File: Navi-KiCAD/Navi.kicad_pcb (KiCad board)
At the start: 4 copper layers, 50 x 40 mm, 203 parts, among them J1 AXK5S80047YG, J2 AXK5S80047YG, J3 473460001, J4 0734120110, J5 0734120110, J6 0734120110, U1 CC1310F128RGZR, U10 Logo, U11 Logo, U12 ATSAME70Q21A-AN, U13 NUF2042XV6T1G, U2 CC1190RGVR, U3 CC2650F128RGZR, U4 CC2592RGVR, U5 MPU-9250, U6 LP5521YQ/NOPB, U7 LPS25HBTR, U8 TPS54232DR, U9 MAX-M8W-0, Y1 9HT11-32.768KDZB-T, Y2 7V-16.000MAHJ-T, Y3 XRCGB24M000F2P00R0, Y5 XRCGB24M000F2P00R0

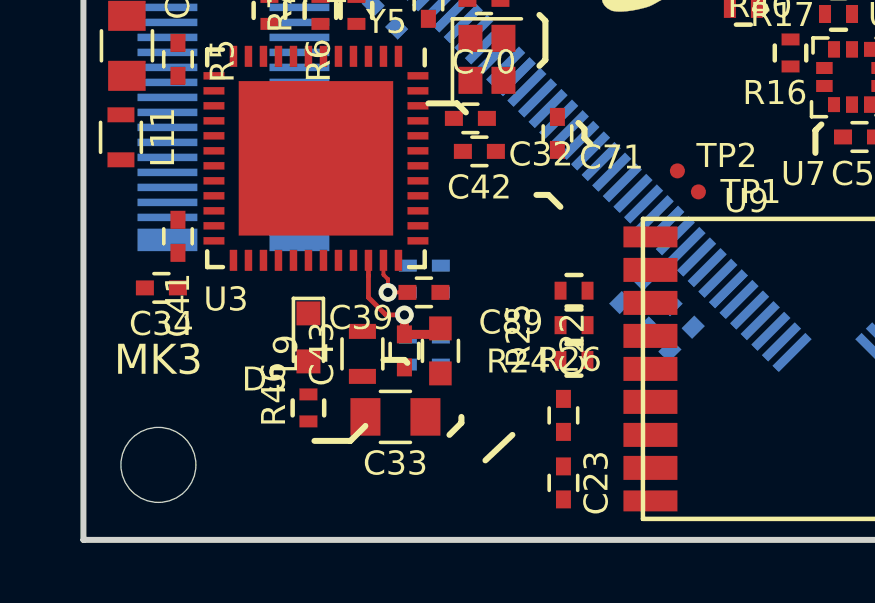
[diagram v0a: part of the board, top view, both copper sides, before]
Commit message: Some BOM consolidation.
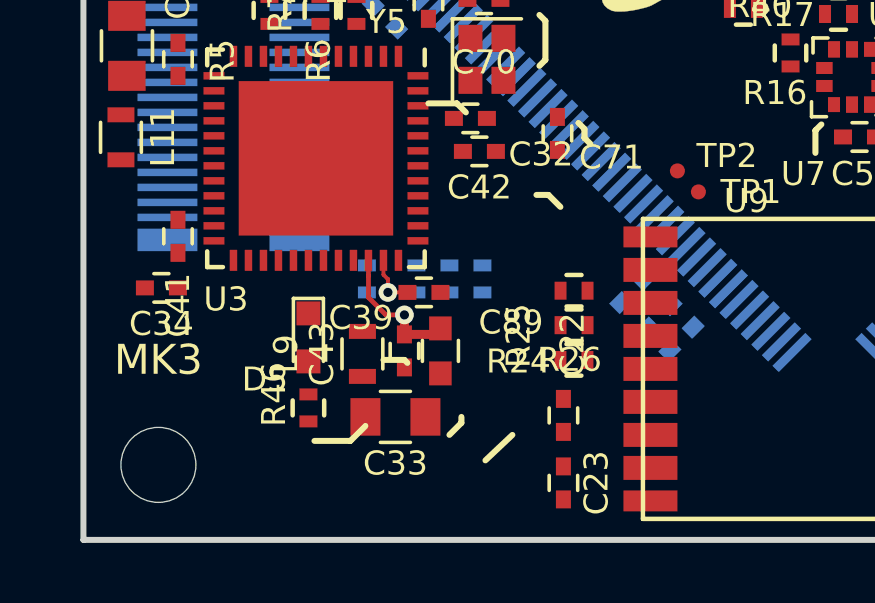
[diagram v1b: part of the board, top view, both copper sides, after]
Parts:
- R40, R41: value DNP -> 0 DNP
- moved U10 28.1 mm to (60.2, 117.8)
- moved R32 2.78 mm to (63.3, 116.3), turned to 270 degrees
- moved R36 2.77 mm to (59.5, 116.3), turned to 90 degrees
- moved R34 0.29 mm to (61.1, 116.3)
- moved R33 0.28 mm to (62.2, 116.3)
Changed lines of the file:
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@@
     (pad 1 np_thru_hole circle (at 0 0) (size 2.5 2.5) (drill 2.5) (layers *.Cu *.Mask))
   )
-  (module Connectors:AXK5S80047YG locked (layer B.Cu)
+  (module Connectors:AXK5S80047YG (layer B.Cu)
     (at 95 105 90)
     (descr AXK5S80047YG)
@@
   )
   (module Symbols:NaviLOGO (layer B.Cu)
-    (at 88.3 118 230)
+    (at 60.2 117.75 230)
     (attr virtual)
     (fp_text reference U10 (at 0 0 230) (layer B.SilkS) hide
@@
       (effects (font (size 0.8 0.8) (thickness 0.13)))
     )
-    (fp_text value DNP (at 0 1.8 180) (layer F.Fab)
+    (fp_text value "0 DNP" (at 0 1.8 180) (layer F.Fab)
       (effects (font (size 1 1) (thickness 0.15)))
     )
@@
       (effects (font (size 0.8 0.8) (thickness 0.13)))
     )
-    (fp_text value DNP (at 0 1.8 180) (layer F.Fab)
+    (fp_text value "0 DNP" (at 0 1.8 180) (layer F.Fab)
       (effects (font (size 1 1) (thickness 0.15)))
     )
@@
   )
   (module Resistors_SMD:R_0402 (layer B.Cu)
-    (at 60.815017 116.307166 270)
+    (at 61.1 116.3 270)
     (descr "Resistor SMD 0402, reflow soldering, Vishay (see dcrcw.pdf)")
     (tags "resistor 0402")
@@
   )
   (module Resistors_SMD:R_0402 (layer B.Cu)
-    (at 61.915018 118.706889 90)
+    (at 63.3 116.3 270)
     (descr "Resistor SMD 0402, reflow soldering, Vishay (see dcrcw.pdf)")
     (tags "resistor 0402")
     (attr smd)
-    (fp_text reference R32 (at 1.949723 0.050526 90) (layer B.SilkS)
+    (fp_text reference R32 (at 1.949723 0.050526 270) (layer B.SilkS)
       (effects (font (size 0.8 0.8) (thickness 0.13)) (justify mirror))
     )
-    (fp_text value 1k (at 0 -1.8 90) (layer B.Fab)
+    (fp_text value 1k (at 0 -1.8 270) (layer B.Fab)
       (effects (font (size 0.9 0.9) (thickness 0.1)) (justify mirror))
     )
@@
     (fp_line (start 0.5 -0.25) (end -0.5 -0.25) (layer B.Fab) (width 0.1))
     (fp_line (start -0.5 -0.25) (end -0.5 0.25) (layer B.Fab) (width 0.1))
-    (pad 2 smd rect (at 0.45 0 90) (size 0.4 0.6) (layers B.Cu B.Paste B.Mask)
+    (pad 2 smd rect (at 0.45 0 270) (size 0.4 0.6) (layers B.Cu B.Paste B.Mask)
       (net 92 "/2.4 GHz Radio/~RESET"))
-    (pad 1 smd rect (at -0.45 0 90) (size 0.4 0.6) (layers B.Cu B.Paste B.Mask)
+    (pad 1 smd rect (at -0.45 0 270) (size 0.4 0.6) (layers B.Cu B.Paste B.Mask)
       (net 118 /2.4_RESET_EXT))
     (model Resistors_SMD.3dshapes/R_0402.wrl
@@
   )
   (module Resistors_SMD:R_0402 (layer B.Cu)
-    (at 60.815017 118.706889 270)
+    (at 59.45 116.3 90)
     (descr "Resistor SMD 0402, reflow soldering, Vishay (see dcrcw.pdf)")
     (tags "resistor 0402")
     (attr smd)
-    (fp_text reference R36 (at 2.000277 -2.050526 270) (layer B.SilkS)
+    (fp_text reference R36 (at 2.000277 -2.050526 90) (layer B.SilkS)
       (effects (font (size 0.8 0.8) (thickness 0.13)) (justify mirror))
     )
-    (fp_text value 100k (at 0 -1.8 270) (layer B.Fab)
+    (fp_text value 100k (at 0 -1.8 90) (layer B.Fab)
       (effects (font (size 0.9 0.9) (thickness 0.1)) (justify mirror))
     )
@@
     (fp_line (start 0.5 -0.25) (end -0.5 -0.25) (layer B.Fab) (width 0.1))
     (fp_line (start -0.5 -0.25) (end -0.5 0.25) (layer B.Fab) (width 0.1))
-    (pad 2 smd rect (at 0.45 0 270) (size 0.4 0.6) (layers B.Cu B.Paste B.Mask)
+    (pad 2 smd rect (at 0.45 0 90) (size 0.4 0.6) (layers B.Cu B.Paste B.Mask)
       (net 14 +3V3))
-    (pad 1 smd rect (at -0.45 0 270) (size 0.4 0.6) (layers B.Cu B.Paste B.Mask)
+    (pad 1 smd rect (at -0.45 0 90) (size 0.4 0.6) (layers B.Cu B.Paste B.Mask)
       (net 92 "/2.4 GHz Radio/~RESET"))
     (model Resistors_SMD.3dshapes/R_0402.wrl
@@
   )
   (module Resistors_SMD:R_0402 (layer B.Cu)
-    (at 61.915544 116.307166 270)
+    (at 62.2 116.3 270)
     (descr "Resistor SMD 0402, reflow soldering, Vishay (see dcrcw.pdf)")
     (tags "resistor 0402")

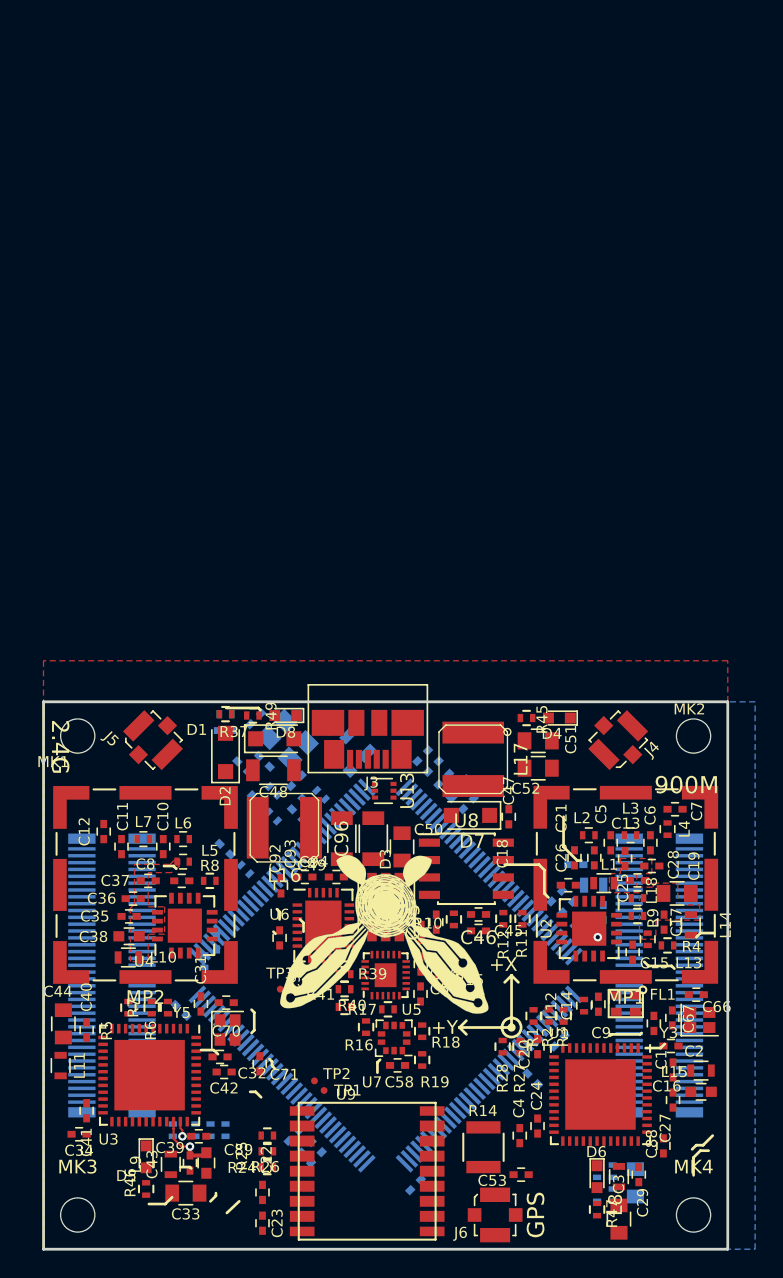
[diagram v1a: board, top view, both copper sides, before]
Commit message: Completed key routing.
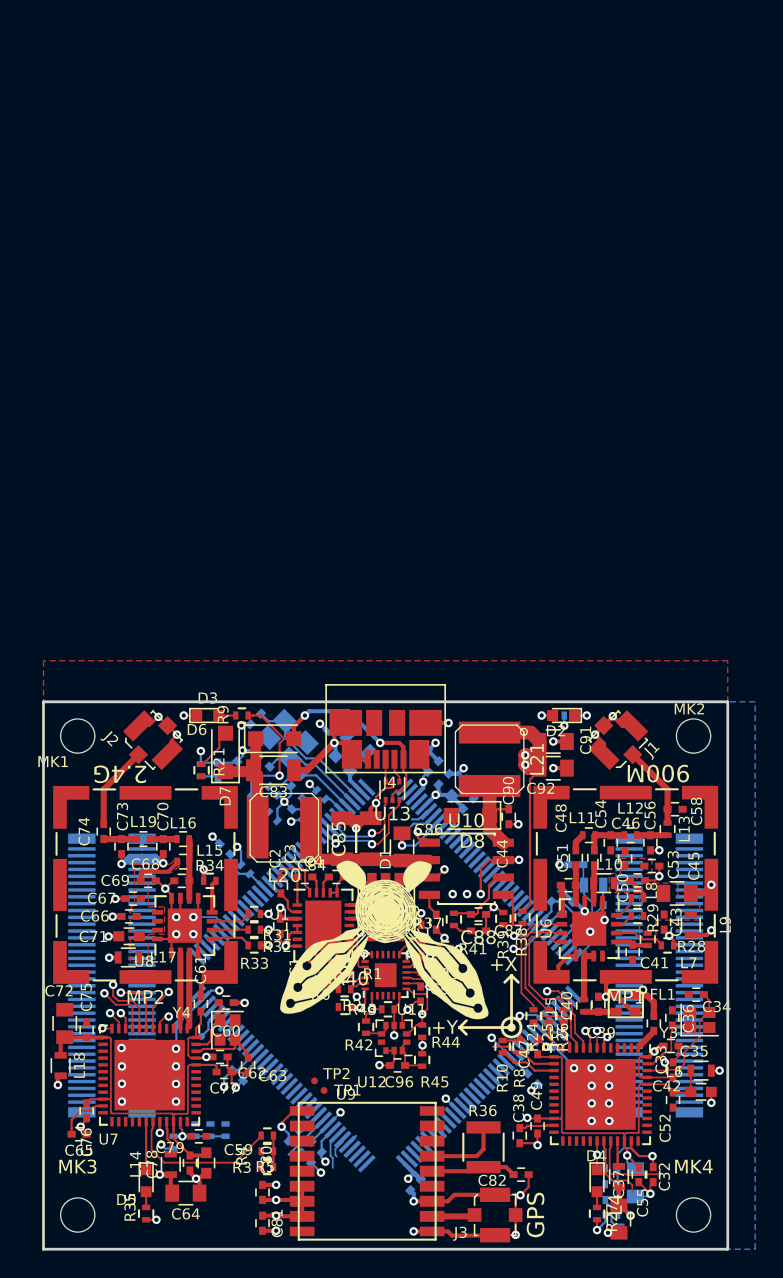
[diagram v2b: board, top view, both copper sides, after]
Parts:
- C69: renamed from C37; value 1n -> 0.01u
- D4: renamed from D6; value MF-LED-0603-RED -> MF-LED-0603-GREEN
- R17: renamed from R20; value 5.6k -> ERJ-2RKF5761X
- R40: renamed from R42; moved to F.Cu
- R7: renamed from R45; moved to B.Cu
- TP3: moved to B.Cu
- moved R31 11.5 mm to (65.4, 100.5), turned to 0 degrees
- moved C25 9.87 mm to (64.2, 112.3), turned to 315 degrees
- moved R33 8.77 mm to (65.4, 102.8), turned to 0 degrees
- moved R40 8.75 mm to (70.4, 105.3)
- moved R32 8.50 mm to (65.4, 101.7), turned to 0 degrees
- moved TP3 6.71 mm to (61.5, 109.5)
- moved D3 5.70 mm to (62.0, 86.0), turned to 0 degrees
- moved R22 4.48 mm to (61.5, 90.0), turned to 270 degrees
- moved R21 4.46 mm to (61.5, 90.0), turned to 90 degrees
- moved C30 2.95 mm to (62.8, 90.0), turned to 90 degrees
- moved R11 2.35 mm to (91.5, 121.4), turned to 0 degrees
- moved R7 2.31 mm to (87.6, 86.0), turned to 180 degrees
- moved R41 2.26 mm to (79.3, 103.0)
- moved C32 2.23 mm to (94.5, 119.5), turned to 270 degrees
- moved R13 1.95 mm to (91.5, 119.1), turned to 0 degrees
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- renumbered C91 to C1, C63 to C10, C74 to C11, C69 to C12, C87 to C13, C65 to C14, C73 to C15, C75 to C16, C76 to C17, C59 to C18, C77 to C19, C92 to C2, C78 to C20, C60 to C21, C79 to C22, C80 to C23, C81 to C24, C82 to C25, C83 to C26, C84 to C27, C85 to C28, C86 to C29, C93 to C3, C90 to C30, C61 to C31, C88 to C32, C1 to C33, C66 to C34, C2 to C35, C67 to C36, C3 to C37, C4 to C38, C9 to C39, C94 to C4, C14 to C40, C15 to C41, C16 to C42, C17 to C43, C18 to C44, C19 to C45, C13 to C46, C20 to C47, C21 to C48, C24 to C49, C62 to C5, C25 to C50, C26 to C51, C27 to C52, C28 to C53, C5 to C54, C29 to C55, C6 to C56, C30 to C57, C7 to C58, C89 to C59, C57 to C6, C70 to C60, C31 to C61, C32 to C62, C71 to C63, C33 to C64, C34 to C65, C35 to C66, C36 to C67, C8 to C68, C64 to C7, C10 to C70, C38 to C71, C44 to C72, C11 to C73, C12 to C74, C40 to C75, C41 to C76, C42 to C77, C43 to C78, C39 to C79, C68 to C8, C22 to C80, C23 to C81, C53 to C82, C48 to C83, C49 to C84, C96 to C85, C50 to C86, C45 to C87, C46 to C88, C95 to C89, C72 to C9, C47 to C90, C51 to C91, C52 to C92, C54 to C93, C55 to C94, C56 to C95, C58 to C96, D3 to D1, D4 to D2, D8 to D3, D1 to D6, D2 to D7, D7 to D8, J4 to J1, J5 to J2, J6 to J3, J3 to J4, J1 to J5, J2 to J6, L19 to L1, L1 to L10, L2 to L11, L3 to L12, L4 to L13, L9 to L14, L5 to L15, L6 to L16, L10 to L17, L11 to L18, L7 to L19, L20 to L2, L16 to L20, L17 to L21, L21 to L3, L8 to L4, L12 to L5, L15 to L6, L13 to L7, L18 to L8, L14 to L9, R39 to R1, R28 to R10, R29 to R11, R30 to R12, R31 to R13, R32 to R14, R33 to R15, R34 to R16, R21 to R18, R22 to R19, R40 to R2, R23 to R20, R37 to R21, R38 to R22, R35 to R23, R1 to R24, R2 to R25, R3 to R26, R47 to R27, R4 to R28, R9 to R29, R24 to R3, R36 to R30, R5 to R31, R6 to R32, R7 to R33, R8 to R34, R46 to R35, R14 to R36, R10 to R37, R11 to R38, R12 to R39, R25 to R4, R15 to R41, R16 to R42, R17 to R43, R18 to R44, R19 to R45, R26 to R5, R41 to R6, R27 to R8, R49 to R9, U6 to U1, U8 to U10, U5 to U11, U7 to U12, U10 to U2, U11 to U3, U12 to U4, U1 to U5, U2 to U6, U3 to U7, U4 to U8, Y5 to Y4
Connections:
- J5 pad 1: Net-(J1-Pad1) -> +BATT
- J5 pad 3: Net-(J1-Pad3) -> +BATT
- J5 pad 5: Net-(J1-Pad5) -> GND
- J5 pad 7: Net-(J1-Pad7) -> GND
- L9 pad 1: /900MHz Radio/VDDS_CC1310 -> +3V3
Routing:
- net GND: track 2.33 -> 203.7 mm, vias 1 -> 90
- net +3V3: track 0.07 -> 77.0 mm, vias 0 -> 26
- net /900MHz Radio/VDDS_CC1310: track 0.00 -> 28.9 mm, vias 0 -> 2
- net VUSB: track 0.00 -> 26.1 mm, vias 0 -> 3
- net Net-(C12-Pad1): track 0.00 -> 24.2 mm, vias 0 -> 7
- net /2.4 GHz Radio/VDDS_CC2650: track 4.61 -> 28.7 mm, vias 1 -> 0
- net /900MHz Radio/VDDR_CC1310: track 0.00 -> 22.7 mm, vias 0 -> 2
- net /2.4 GHz Radio/VDDR_CC2650: track 0.00 -> 19.7 mm, vias 0 -> 2
- net /CPU_RESET_2.4: track 0.00 -> 11.4 mm
- net Net-(C84-Pad1): track 0.00 -> 10.6 mm
- net /900MHz Radio/~RESET: track 0.00 -> 10.5 mm, vias 0 -> 1
- net Net-(C14-Pad2): track 0.00 -> 10.3 mm
- net Net-(C90-Pad2): track 0.00 -> 9.69 mm, vias 0 -> 2
- net Net-(R26-Pad1): track 0.00 -> 9.55 mm
- net Net-(R24-Pad1): track 0.00 -> 9.07 mm
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- removed copper zone on In2.Cu, net Net-(C84-Pad1)

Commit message: Some more GNC processor routing
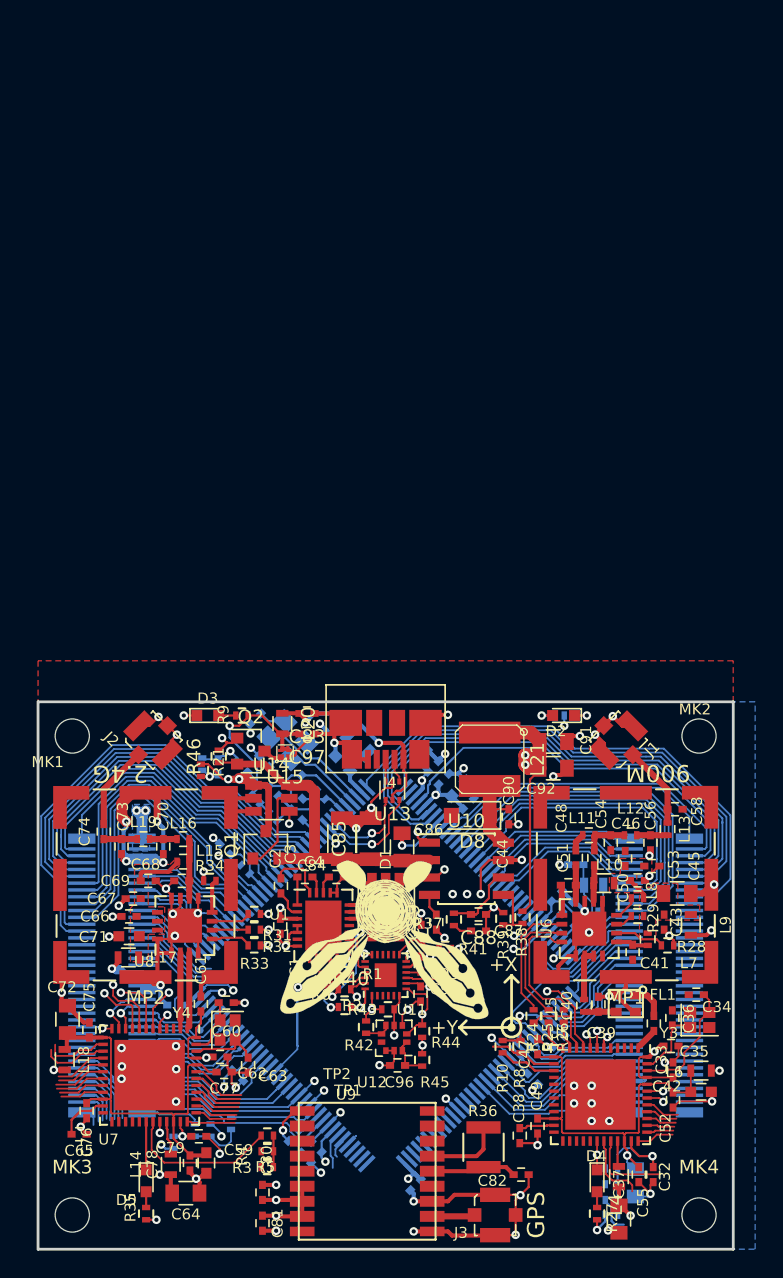
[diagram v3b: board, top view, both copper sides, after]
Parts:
- removed D6, D7: SS24FL, Diodes_SMD:D_SOD-123F
- added C97: 0.1u, Capacitors_SMD:C_0402, F.Cu at (69.2, 87.3)
- added Q1: IRLML5203PbF, TO_SOT_Packages_SMD:SOT-23, F.Cu at (66.2, 95.5)
- added Q2: IRLML5203PbF, TO_SOT_Packages_SMD:SOT-23, F.Cu at (65.2, 88.6)
- added R46: 470k, Resistors_SMD:R_0402, F.Cu at (62.8, 89.0)
- added U14: LTC4412ES6, TO_SOT_Packages_SMD:TSOT-23-6_MK06A, F.Cu at (66.7, 92.0)
- added U15: MIC94082YFT, SMD_Packages:TMLF085085D-4LD-9, F.Cu at (67.7, 88.8)
- C83: value GRM31CR61H106MA12L -> 0.01u; footprint Capacitors_SMD:C_1206 -> Capacitors_SMD:C_0402
- L20: value 74404052100 -> BLM18HE152SN1D; footprint Inductors:Inductor_Wurth_LQS-5020 -> Inductors_SMD:L_0603
- L9: value CIH10T22NJNC -> BLM18HE152SN1D
- moved L20 7.61 mm to (67.5, 86.6), turned to 270 degrees
- moved C83 4.82 mm to (69.2, 85.8), turned to 180 degrees
- moved R16 2.65 mm to (63.7, 115.8)
- moved R14 2.25 mm to (61.0, 116.3)
- moved C19 1.20 mm to (59.6, 107.2), turned to 180 degrees
- moved C10 0.83 mm to (90.1, 100.3), turned to 0 degrees
- moved L18 0.52 mm to (51.5, 111.2)
- moved R22 0.46 mm to (61.6, 89.5)
- moved TP3 0.46 mm to (61.5, 109.0)
- moved MK2 0.40 mm to (97.9, 87.5)
- moved MK4 0.40 mm to (97.9, 122.5)
- moved MK1 0.40 mm to (52.1, 87.5)
- moved MK3 0.40 mm to (52.1, 122.5)
- moved C72 0.36 mm to (51.8, 108.2)
- moved C30 0.25 mm to (62.8, 89.8)
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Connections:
- C83 pad 1: Net-(C83-Pad1) -> GND
- C83 pad 2: GND -> Net-(C83-Pad2)
- J4 pad 1: VUSB -> Net-(C83-Pad2)
- J5 pad 10: Net-(J5-Pad10) -> /Connectors/PC24
- J5 pad 11: Net-(J5-Pad11) -> /Connectors/PC19
- J5 pad 12: Net-(J5-Pad12) -> /Connectors/PD2
- J5 pad 13: Net-(J5-Pad13) -> /Connectors/PA30
- J5 pad 14: Net-(J5-Pad14) -> /Connectors/PD5
- J5 pad 15: Net-(J5-Pad15) -> /Connectors/PD8
- J5 pad 16: Net-(J5-Pad16) -> /Connectors/PC22
- J5 pad 17: Net-(J5-Pad17) -> /Connectors/PA28
- J5 pad 18: Net-(J5-Pad18) -> /Connectors/PC21
- J5 pad 19: Net-(J5-Pad19) -> /Connectors/PC18
- J5 pad 2: Net-(J5-Pad2) -> /Connectors/PD4
- J5 pad 20: Net-(J5-Pad20) -> /Connectors/PD6
- J5 pad 21: Net-(J5-Pad21) -> /Connectors/PD9
- J5 pad 22: Net-(J5-Pad22) -> /Connectors/PC20
- J5 pad 23: Net-(J5-Pad23) -> /Connectors/PB5
- J5 pad 24: Net-(J5-Pad24) -> /Connectors/PD7
- J5 pad 26: Net-(J5-Pad26) -> /Connectors/PD1
- J5 pad 28: Net-(J5-Pad28) -> /Connectors/PC25
- J5 pad 33: Net-(J5-Pad33) -> /Connectors/PD15
- J5 pad 39: Net-(J5-Pad39) -> +3V3
- J5 pad 4: Net-(J5-Pad4) -> /Connectors/PC23
- J5 pad 41: Net-(J5-Pad41) -> +3V3
- J5 pad 43: Net-(J5-Pad43) -> GND
- J5 pad 45: Net-(J5-Pad45) -> GND
- J5 pad 47: Net-(J5-Pad47) -> /CPU-SCK
- J5 pad 49: Net-(J5-Pad49) -> /CPU-SDA
- J5 pad 51: Net-(J5-Pad51) -> /Connectors/PB4
- J5 pad 53: Net-(J5-Pad53) -> /Connectors/PC17
- J5 pad 55: Net-(J5-Pad55) -> /Connectors/PA0
- J5 pad 56: Net-(J5-Pad56) -> /Connectors/2.4-DIO-7
- J5 pad 57: Net-(J5-Pad57) -> /Connectors/PD10
- J5 pad 59: Net-(J5-Pad59) -> /Connectors/PC16
- J5 pad 6: Net-(J5-Pad6) -> /Connectors/PD3
- J5 pad 61: Net-(J5-Pad61) -> /Connectors/PA1
- J5 pad 63: Net-(J5-Pad63) -> /Connectors/PD11
- J5 pad 65: Net-(J5-Pad65) -> /Connectors/PC14
- J5 pad 67: Net-(J5-Pad67) -> /Connectors/PC11
- J5 pad 69: Net-(J5-Pad69) -> /Connectors/PC10
- J5 pad 71: Net-(J5-Pad71) -> /Connectors/PB7
- J5 pad 73: Net-(J5-Pad73) -> /Connectors/PB12
- J5 pad 75: Net-(J5-Pad75) -> /Connectors/PC9
- J5 pad 77: Net-(J5-Pad77) -> /Connectors/PC8
- J5 pad 79: Net-(J5-Pad79) -> /2.4_RESET_EXT
- J5 pad 8: Net-(J5-Pad8) -> /Connectors/PA29
- J5 pad 9: Net-(J5-Pad9) -> /Connectors/PA31
- J6 pad 1: Net-(J6-Pad1) -> /Connectors/PC0
- J6 pad 10: Net-(J6-Pad10) -> /Connectors/PB0
- J6 pad 11: Net-(J6-Pad11) -> /Connectors/PE1
- J6 pad 12: Net-(J6-Pad12) -> /Connectors/PA20
- J6 pad 13: Net-(J6-Pad13) -> /Connectors/PE2
- J6 pad 14: Net-(J6-Pad14) -> /Connectors/PC29
- J6 pad 15: Net-(J6-Pad15) -> /Connectors/PB13
- J6 pad 16: Net-(J6-Pad16) -> /Connectors/PC30
- J6 pad 18: Net-(J6-Pad18) -> /Connectors/PC31
- J6 pad 2: Net-(J6-Pad2) -> /Connectors/PC12
- J6 pad 20: Net-(J6-Pad20) -> /Connectors/PC26
- J6 pad 22: Net-(J6-Pad22) -> /Connectors/PC27
- J6 pad 24: Net-(J6-Pad24) -> /Connectors/PA21
- J6 pad 26: Net-(J6-Pad26) -> /Connectors/PB3
- J6 pad 3: Net-(J6-Pad3) -> /Connectors/PE3
- J6 pad 30: Net-(J6-Pad30) -> /Connectors/PA16
- J6 pad 32: Net-(J6-Pad32) -> /Connectors/PA22
- J6 pad 34: Net-(J6-Pad34) -> /Connectors/PC1
- J6 pad 36: Net-(J6-Pad36) -> /Connectors/PC2
- J6 pad 38: Net-(J6-Pad38) -> /Connectors/PC3
- J6 pad 4: Net-(J6-Pad4) -> /Connectors/PC15
- J6 pad 40: Net-(J6-Pad40) -> /Connectors/PC4
- J6 pad 42: Net-(J6-Pad42) -> /Connectors/PA13
- J6 pad 5: Net-(J6-Pad5) -> /Connectors/PE0
- J6 pad 6: Net-(J6-Pad6) -> /Connectors/PC13
- J6 pad 60: Net-(J6-Pad60) -> /Connectors/PA23
- J6 pad 62: Net-(J6-Pad62) -> /Connectors/PD27
- J6 pad 64: Net-(J6-Pad64) -> /Connectors/PC7
- J6 pad 66: Net-(J6-Pad66) -> /Connectors/PA15
- J6 pad 68: Net-(J6-Pad68) -> /Connectors/PA14
- J6 pad 7: Net-(J6-Pad7) -> /Connectors/PD0
- J6 pad 70: Net-(J6-Pad70) -> /Connectors/PD25
- J6 pad 72: Net-(J6-Pad72) -> /Connectors/PD26
- J6 pad 74: Net-(J6-Pad74) -> /Connectors/PC6
- J6 pad 76: Net-(J6-Pad76) -> /Connectors/PD24
- J6 pad 78: Net-(J6-Pad78) -> /Connectors/PA24
- J6 pad 8: Net-(J6-Pad8) -> /Connectors/PB1
- J6 pad 9: Net-(J6-Pad9) -> /Connectors/PD31
- L20 pad 1: Net-(C83-Pad1) -> Net-(C83-Pad2)
- L20 pad 2: Net-(C84-Pad1) -> VUSB
- U13 pad 5: VUSB -> Net-(C83-Pad2)
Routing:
- net /Connectors/PE2: track 1.95 -> 42.2 mm
- net /Connectors/PB13: track 0.00 -> 39.5 mm
- net /Connectors/PE1: track 1.48 -> 39.9 mm
- net GND: track 203.7 -> 240.3 mm, vias 90 -> 87
- net /Connectors/PD31: track 0.00 -> 35.9 mm
- net /Connectors/PC25: track 0.00 -> 35.2 mm
- net /Connectors/PD1: track 0.00 -> 33.8 mm
- net /Connectors/PD0: track 0.00 -> 31.8 mm
- net /Connectors/PD2: track 0.00 -> 29.4 mm
- net /Connectors/PE0: track 0.00 -> 29.3 mm
- net /Connectors/PC24: track 0.00 -> 27.9 mm
- net /Connectors/PC27: track 0.00 -> 27.0 mm
- net /Connectors/PA29: track 0.00 -> 26.5 mm
- net /Connectors/PC26: track 0.00 -> 25.6 mm
- net /Connectors/PD3: track 0.00 -> 25.1 mm
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- added copper zone on B.Cu, net +BATT
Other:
- board size 50 x 40 mm -> 50.8 x 40 mm
